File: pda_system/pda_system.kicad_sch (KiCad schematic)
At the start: 4 parts, among them U1 STM32F103C8Tx, Y1 8Mhz

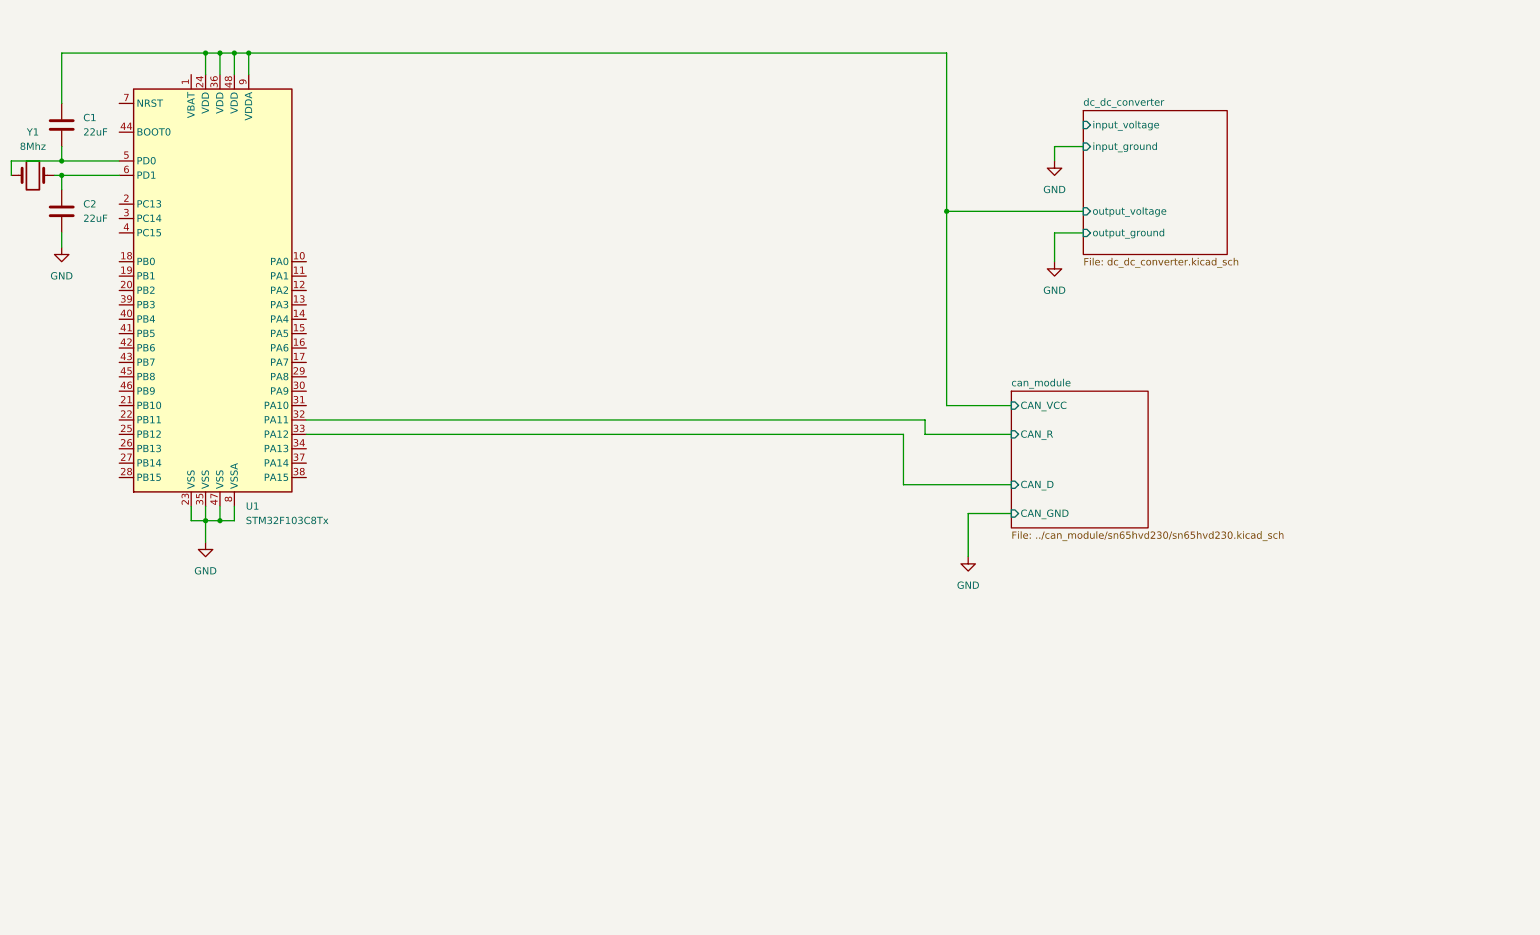
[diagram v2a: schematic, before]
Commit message: updated the network labels along with global nets. Also added programming/debugging port to schematic.
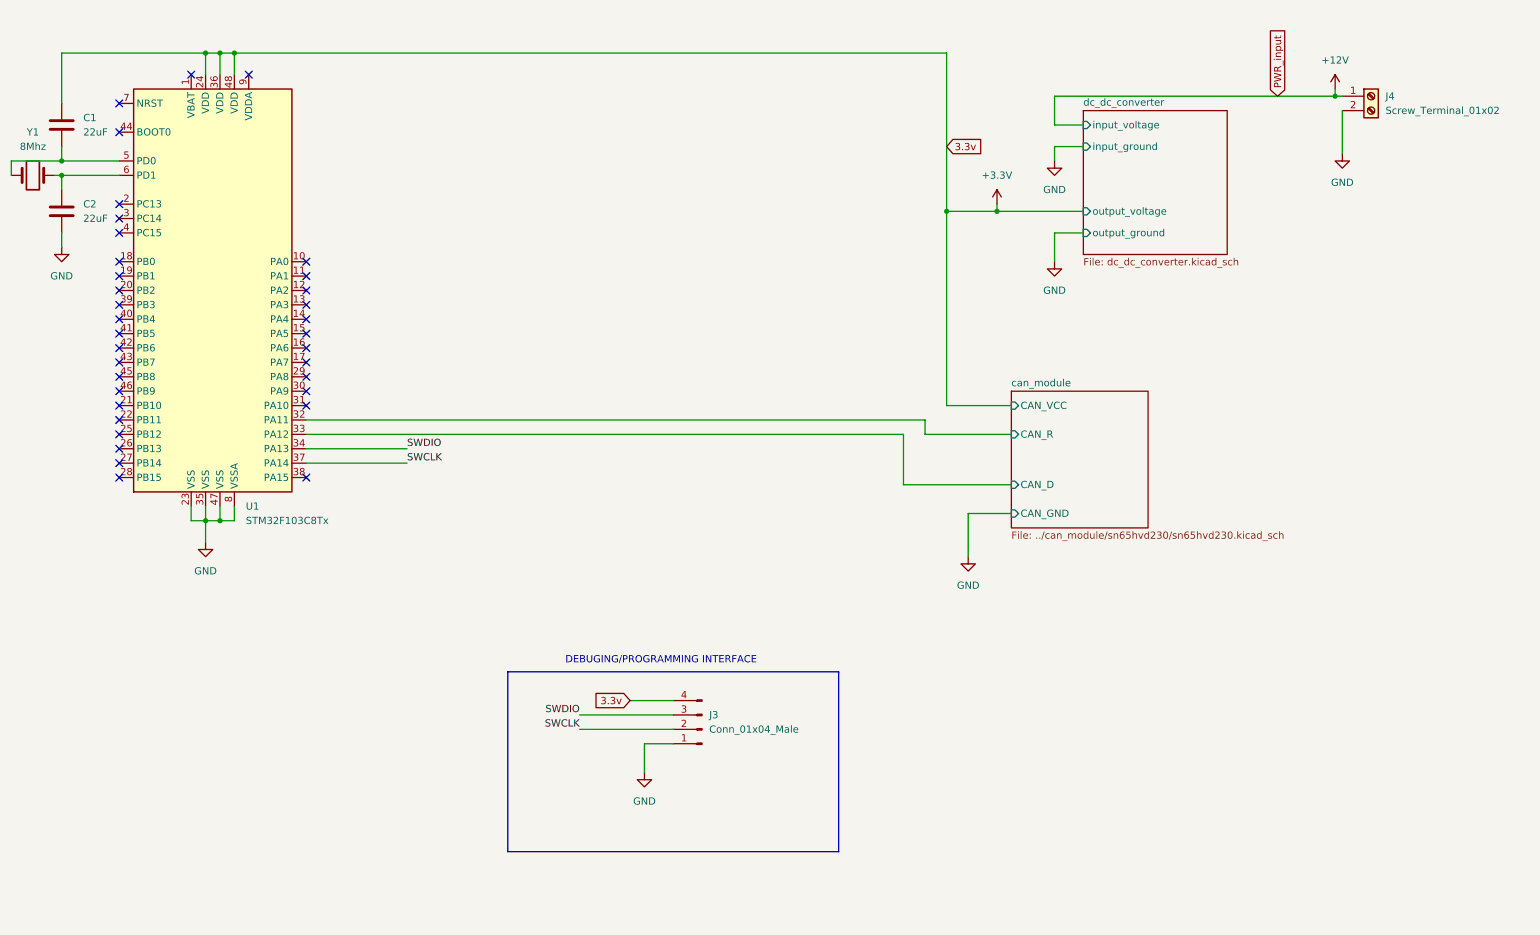
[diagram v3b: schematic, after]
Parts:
- added J3: Conn_01x04_Male, symbol Connector:Conn_01x04_Male
- added J4: Screw_Terminal_01x02, symbol Connector:Screw_Terminal_01x02
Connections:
- net GND: now also J3.1 (Pin_1), J4.2 (Pin_2)
- net SWDIO: now reaches U1.34 (PA13)
- net SWDIO: now also J3.3 (Pin_3)
- net SWCLK: now reaches U1.37 (PA14)
- net SWCLK: now also J3.2 (Pin_2)
- net can_module/CAN_VCC renamed +3V3
- net +3V3: now also J3.4 (Pin_4); no longer U1.9 (VDDA)
- new net +12V: J4.1 (Pin_1)
- no-connect marks 0 -> 35
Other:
- note added: "DEBUGING/PROGRAMMING INTERFACE"

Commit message: fixed some connection issues, and imported the bluepill module
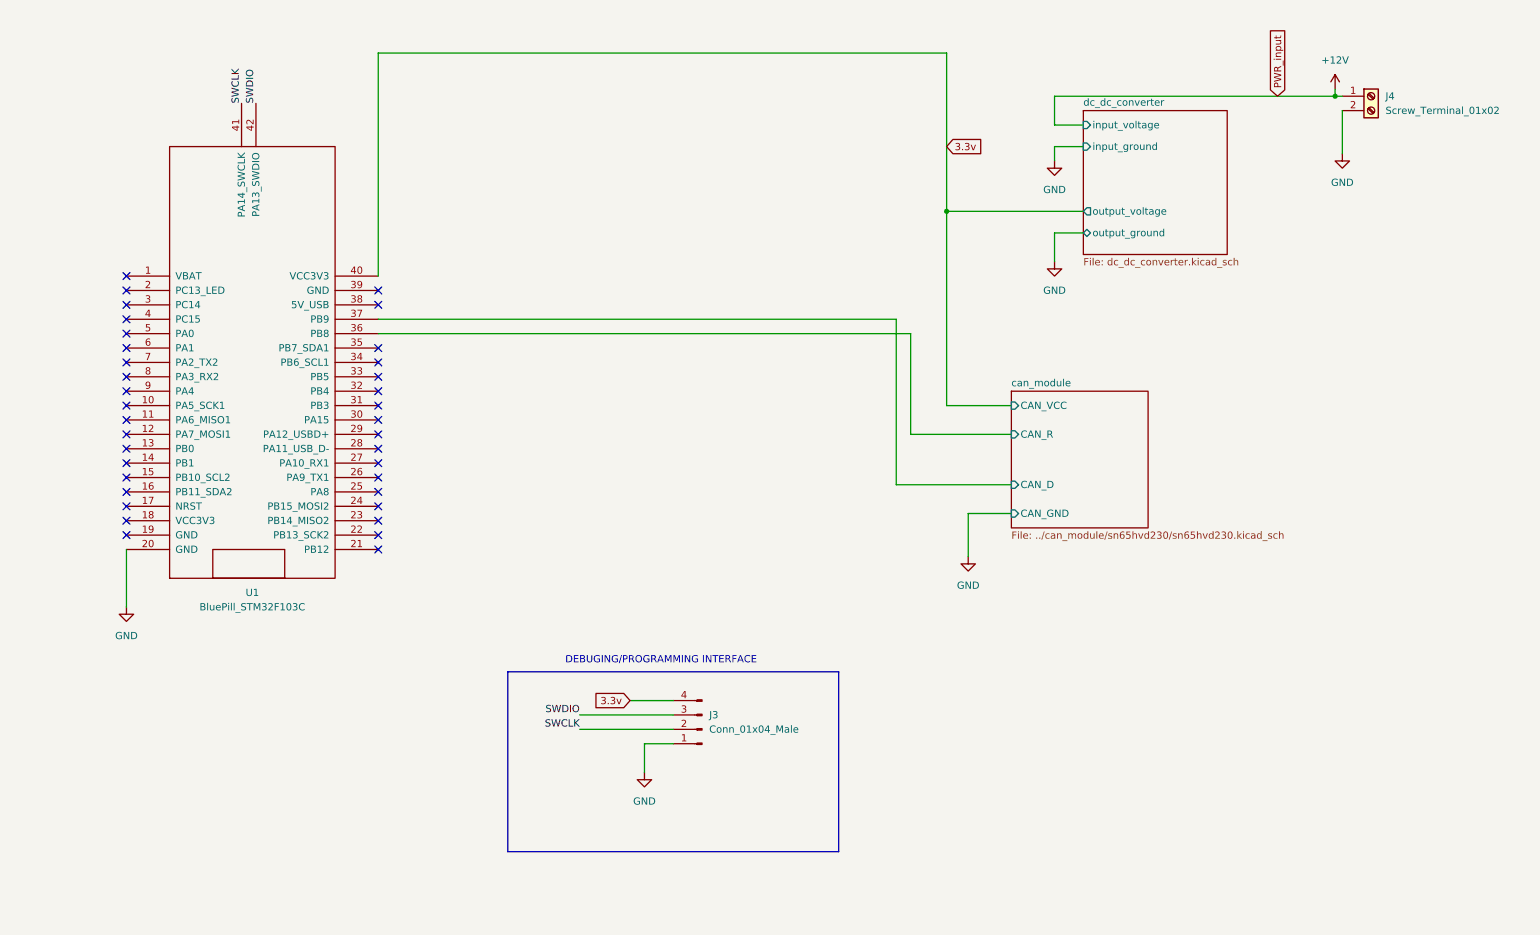
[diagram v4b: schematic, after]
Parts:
- removed C1, C2: 22uF, symbol Device:C
- removed U1: STM32F103C8Tx, Package_QFP:LQFP-48_7x7mm_P0.5mm, symbol MCU_ST_STM32F1:STM32F103C8Tx
- removed Y1: 8Mhz, Crystal:Crystal_HC49-4H_Vertical, symbol Device:Crystal
- added U1: BluePill_STM32F103C, BluePill_breakouts:BluePill_STM32F103C, symbol bluepill_breakouts:BluePill_STM32F103C
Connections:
- net GND: now also U1.20 (GND)
- net SWCLK: now also U1.41 (PA14_SWCLK)
- net SWDIO: now also U1.42 (PA13_SWDIO)
- net can_module/CAN_D: now also U1.37 (PB9)
- net can_module/CAN_R: now also U1.36 (PB8)
- net +3V3 renamed 3.3v
- net 3.3v: now also U1.40 (VCC3V3)
- no-connect marks 35 -> 36

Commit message: fixed two more errors with electrical rules check
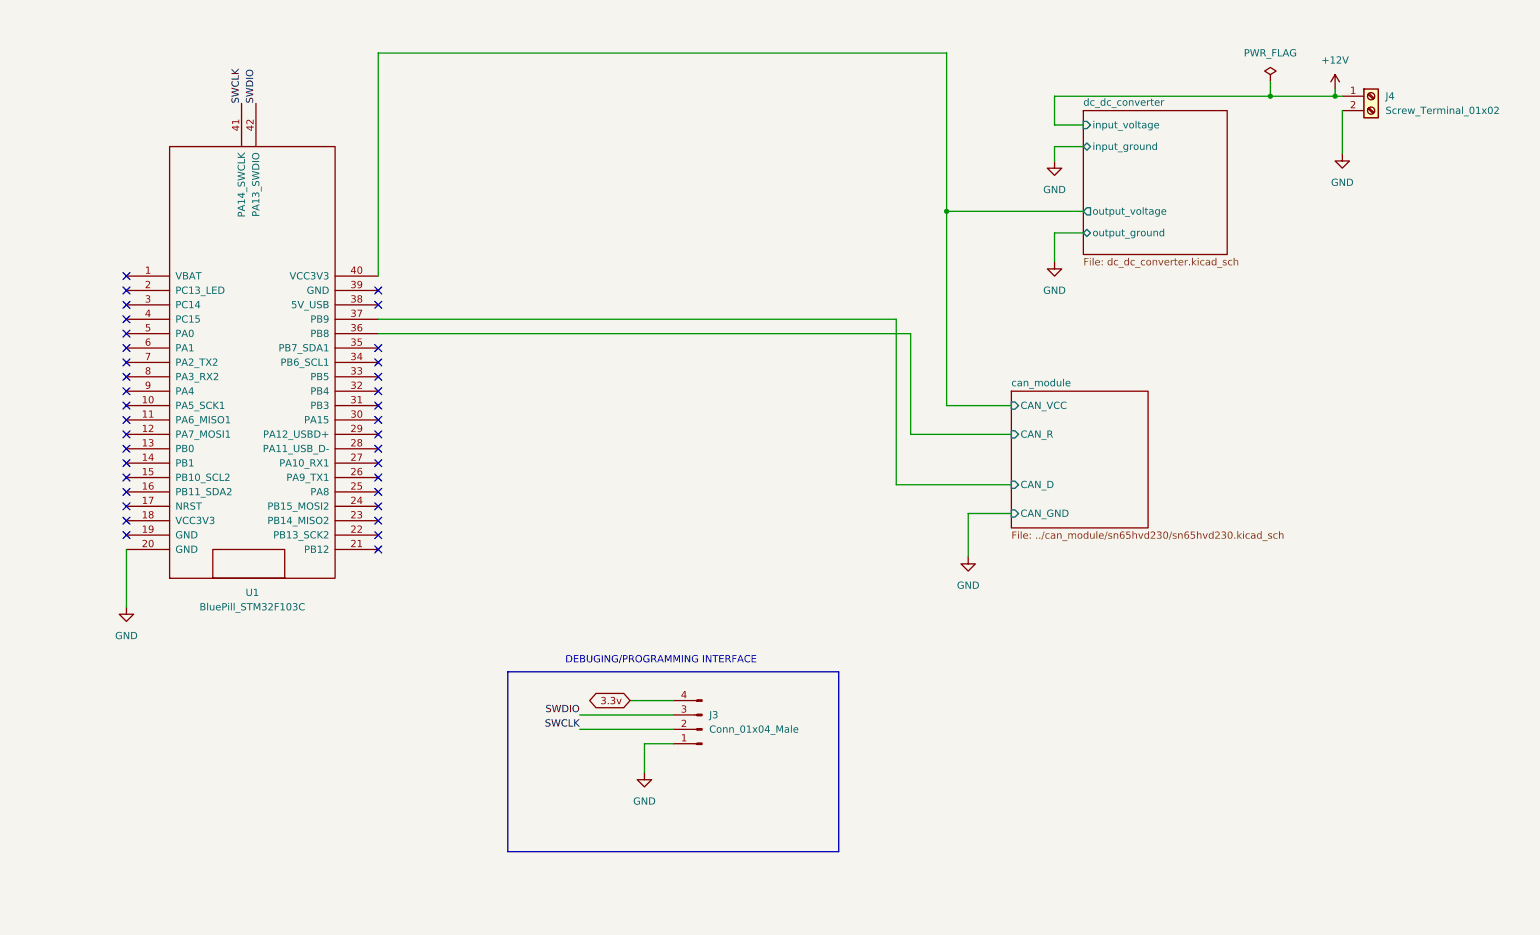
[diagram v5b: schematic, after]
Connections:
- net 3.3v: no longer U1.40 (VCC3V3)
- new net can_module/CAN_VCC: U1.40 (VCC3V3)
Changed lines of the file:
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@@
   (junction (at 191.77 43.18) (diameter 0) (color 0 0 0 0)
+  )
+  (junction (at 248.92 22.86) (diameter 0) (color 0 0 0 0)
   )
   (junction (at 260.35 22.86) (diameter 0) (color 0 0 0 0)
@@
     (stroke (width 0) (type default) (color 0 0 0 0))
   )
-  (wire (pts (xy 260.35 22.86) (xy 210.82 22.86))
+  (wire (pts (xy 260.35 22.86) (xy 248.92 22.86))
     (stroke (width 0) (type default) (color 0 0 0 0))
   )
@@
     (stroke (width 0) (type default) (color 0 0 0 0))
   )
+  (wire (pts (xy 248.92 20.32) (xy 248.92 22.86))
+    (stroke (width 0) (type default) (color 0 0 0 0))
+  )
   (wire (pts (xy 261.62 22.86) (xy 260.35 22.86))
     (stroke (width 0) (type default) (color 0 0 0 0))
@@
   )
   (wire (pts (xy 185.42 82.55) (xy 203.2 82.55))
+    (stroke (width 0) (type default) (color 0 0 0 0))
+  )
+  (wire (pts (xy 248.92 22.86) (xy 210.82 22.86))
     (stroke (width 0) (type default) (color 0 0 0 0))
   )
@@
     (effects (font (size 1.27 1.27)) (justify right bottom))
   )
-  (global_label "3.3v" (shape input) (at 135.89 129.54 180) (fields_autoplaced)
+  (global_label "3.3v" (shape bidirectional) (at 135.89 129.54 180) (fields_autoplaced)
     (effects (font (size 1.27 1.27)) (justify right))
-    (property "Intersheet References" "${INTERSHEET_REFS}" (id 0) (at 129.4855 129.6194 0)
+    (property "Intersheet References" "${INTERSHEET_REFS}" (id 0) (at 129.4855 129.4606 0)
       (effects (font (size 1.27 1.27)) (justify right) hide)
     )
   )
-  (global_label "3.3v" (shape input) (at 191.77 31.75 0) (fields_autoplaced)
-    (effects (font (size 1.27 1.27)) (justify left))
-    (property "Intersheet References" "${INTERSHEET_REFS}" (id 0) (at 198.1745 31.6706 0)
-      (effects (font (size 1.27 1.27)) (justify left) hide)
-    )
-  )
-  (global_label "PWR_input" (shape input) (at 250.19 22.86 90) (fields_autoplaced)
-    (effects (font (size 1.27 1.27)) (justify left))
-    (property "Intersheet References" "${INTERSHEET_REFS}" (id 0) (at 250.1106 10.7102 90)
-      (effects (font (size 1.27 1.27)) (justify left) hide)
-    )
-  )
   (symbol (lib_id "Connector:Screw_Terminal_01x02") (at 266.7 22.86 0) (unit 1)
     (in_bom yes) (on_board yes) (fields_autoplaced)
@@
     (pin "1")
     (pin "2")
+  )
+  (symbol (lib_id "power:PWR_FLAG") (at 248.92 20.32 0) (unit 1)
+    (in_bom yes) (on_board yes) (fields_autoplaced)
+    (property "Reference" "#FLG0101" (id 0) (at 248.92 18.415 0)
+      (effects (font (size 1.27 1.27)) hide)
+    )
+    (property "Value" "PWR_FLAG" (id 1) (at 248.92 15.24 0))
+    (property "Footprint" "" (id 2) (at 248.92 20.32 0)
+      (effects (font (size 1.27 1.27)) hide)
+    )
+    (property "Datasheet" "~" (id 3) (at 248.92 20.32 0)
+      (effects (font (size 1.27 1.27)) hide)
+    )
+    (pin "1")
   )
   (symbol (lib_id "power:GND") (at 210.82 34.29 0) (unit 1)
@@
       (effects (font (size 1.27 1.27)) (justify left))
     )
-    (pin "input_ground" input (at 215.9 31.75 180)
+    (pin "input_ground" bidirectional (at 215.9 31.75 180)
       (effects (font (size 1.27 1.27)) (justify left))
     )
@@
   )
   (symbol_instances
+    (path "/48fc0f63-60a4-496b-b34a-e179f8909f53"
+      (reference "#FLG0101") (unit 1) (value "PWR_FLAG") (footprint "")
+    )
     (path "/4a734e8c-369c-4bb8-b786-a974b034cd31/1c3627f9-1535-4f55-a7b1-ecb389a7d580"
       (reference "#PWR01") (unit 1) (value "GND") (footprint "")
@@
       (reference "#PWR0109") (unit 1) (value "GND") (footprint "")
     )
+    (path "/5ffeb525-fdbf-4755-b592-8d08c6d7cfa4/d3b5210f-4575-4cdb-879a-cce5a3bdb0ec"
+      (reference "#PWR0110") (unit 1) (value "+3.3V") (footprint "")
+    )
     (path "/84e94d67-7ab9-4218-b657-7d37f6b0badb"

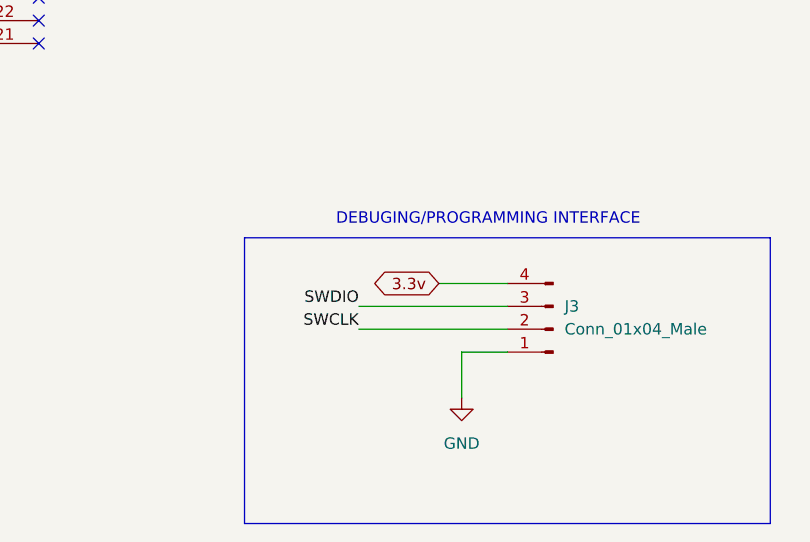
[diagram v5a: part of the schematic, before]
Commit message: minor fixes of ecc issues.
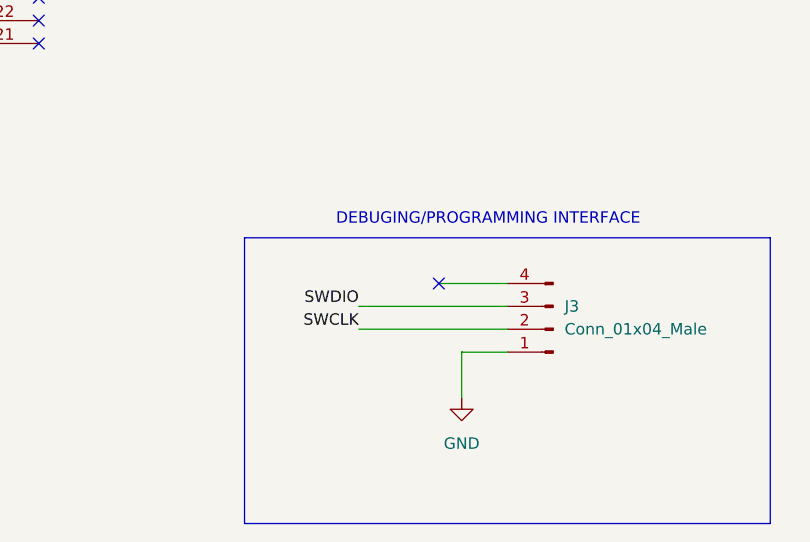
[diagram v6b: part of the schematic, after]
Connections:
- net 3.3v: no longer names the net of J3.4 (Pin_4)
- no-connect marks 36 -> 37
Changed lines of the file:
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@@
   (no_connect (at 46.99 57.15))
   (no_connect (at 46.99 54.61))
+  (no_connect (at 135.89 129.54))
   (polyline (pts (xy 114.3 124.46) (xy 172.72 124.46))
     (stroke (width 0) (type default) (color 0 0 0 0))
@@
   (label "SWDIO" (at 127 132.08 180)
     (effects (font (size 1.27 1.27)) (justify right bottom))
-  )
-  (global_label "3.3v" (shape bidirectional) (at 135.89 129.54 180) (fields_autoplaced)
-    (effects (font (size 1.27 1.27)) (justify right))
-    (property "Intersheet References" "${INTERSHEET_REFS}" (id 0) (at 129.4855 129.4606 0)
-      (effects (font (size 1.27 1.27)) (justify right) hide)
-    )
   )
   (symbol (lib_id "Connector:Screw_Terminal_01x02") (at 266.7 22.86 0) (unit 1)
@@
       (reference "#FLG0101") (unit 1) (value "PWR_FLAG") (footprint "")
     )
-    (path "/4a734e8c-369c-4bb8-b786-a974b034cd31/1c3627f9-1535-4f55-a7b1-ecb389a7d580"
-      (reference "#PWR01") (unit 1) (value "GND") (footprint "")
-    )
     (path "/5ffeb525-fdbf-4755-b592-8d08c6d7cfa4/c382b12a-2eb6-4570-9871-f5e05861e641"
       (reference "#PWR0101") (unit 1) (value "GND") (footprint "")
@@
       (reference "#PWR0102") (unit 1) (value "GND") (footprint "")
     )
-    (path "/5ffeb525-fdbf-4755-b592-8d08c6d7cfa4/70018adf-6148-4891-83ef-ee27182e14a7"
-      (reference "#PWR0103") (unit 1) (value "GND") (footprint "")
-    )
-    (path "/5ffeb525-fdbf-4755-b592-8d08c6d7cfa4/09991386-3ca9-41ea-998b-6b5a7f1d0820"
-      (reference "#PWR0104") (unit 1) (value "GND") (footprint "")
-    )
     (path "/5ffeb525-fdbf-4755-b592-8d08c6d7cfa4/9418a57a-e863-4341-8372-869e517e0a51"
       (reference "#PWR0105") (unit 1) (value "GND") (footprint "")
@@
       (reference "#PWR0109") (unit 1) (value "GND") (footprint "")
     )
-    (path "/5ffeb525-fdbf-4755-b592-8d08c6d7cfa4/d3b5210f-4575-4cdb-879a-cce5a3bdb0ec"
-      (reference "#PWR0110") (unit 1) (value "+3.3V") (footprint "")
-    )
     (path "/84e94d67-7ab9-4218-b657-7d37f6b0badb"
